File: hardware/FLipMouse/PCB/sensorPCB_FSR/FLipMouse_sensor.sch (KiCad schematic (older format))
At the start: 9 parts, among them J1 Conn_02x05_Odd_Even, J2 FSR1, J3 FSR1, J4 FSR2, J5 FSR2, J6 FSR3, J7 FSR3, J8 FSR4, J9 FSR4

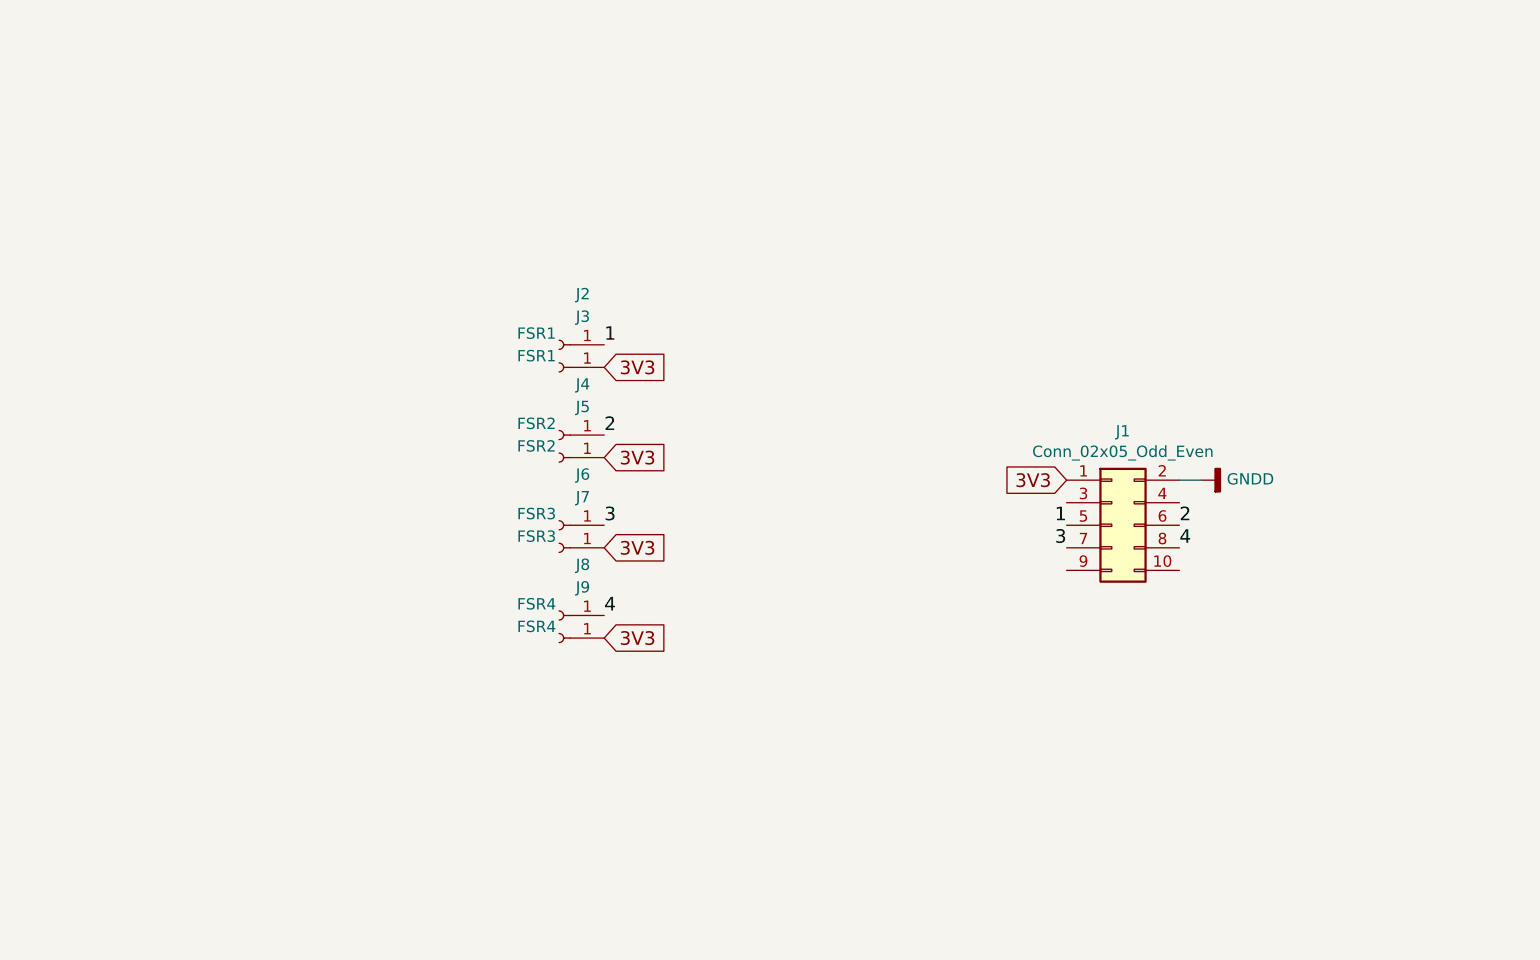
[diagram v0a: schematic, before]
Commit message: Added MEMS microphone to sensor PCB for voice recognition. Added production information
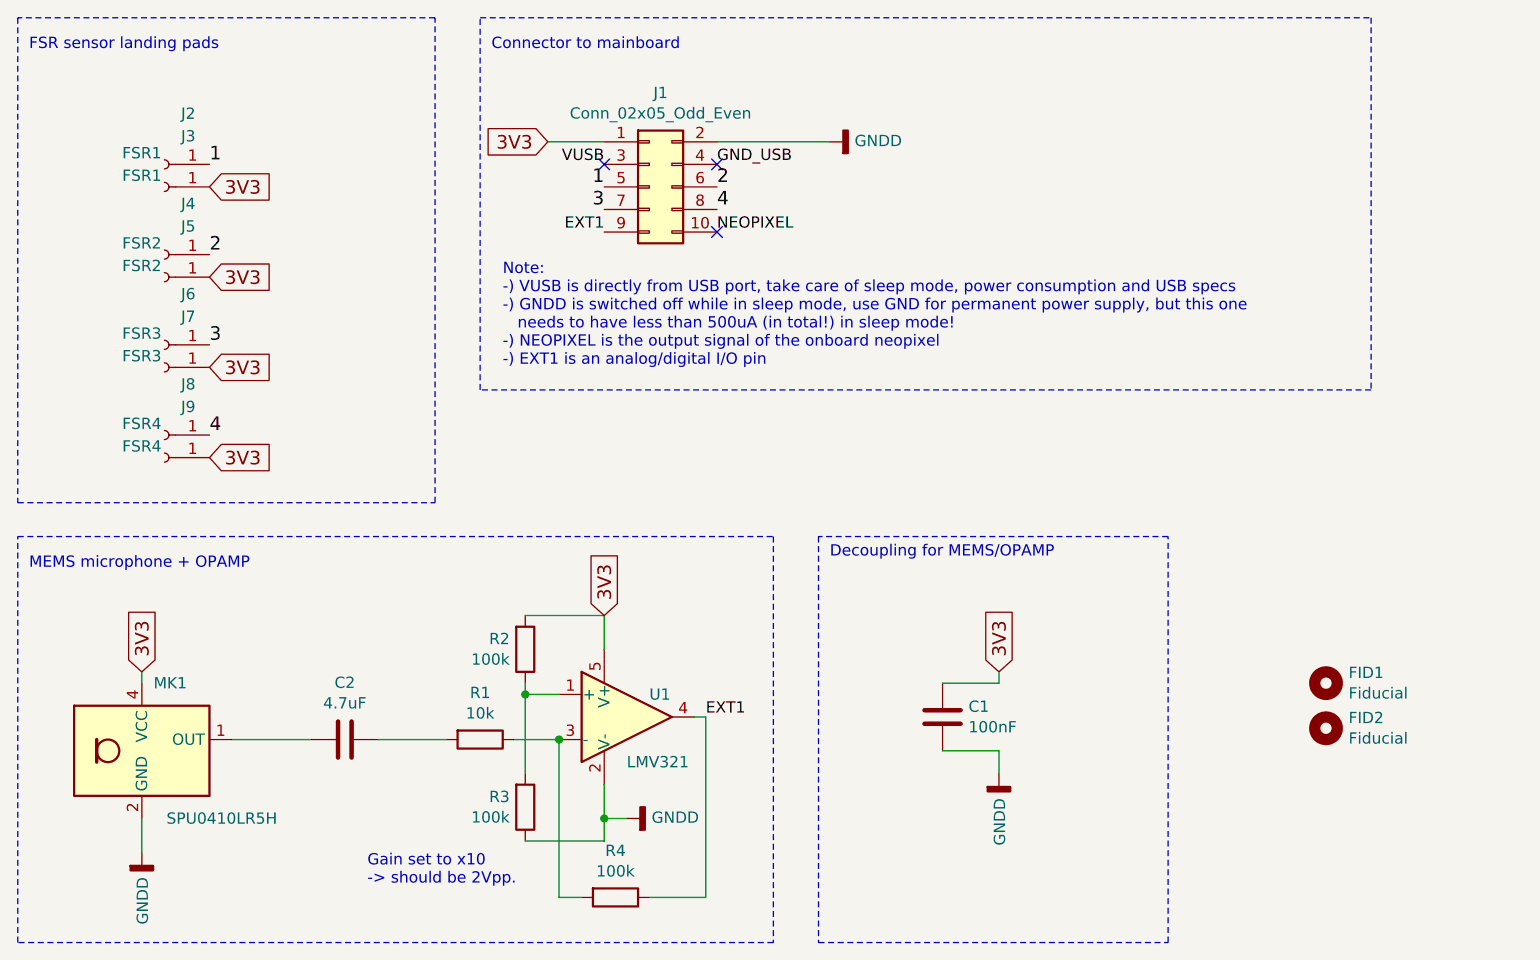
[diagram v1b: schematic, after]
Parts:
- added C1: 100nF, Capacitor_SMD:C_0603_1608Metric, symbol Device:C
- added C2: 4.7uF, Capacitor_SMD:C_0603_1608Metric, symbol Device:C
- added FID1, FID2: Fiducial, Fiducial:Fiducial_0.5mm_Dia_1mm_Outer, symbol Mechanical:MountingHole
- added MK1: SPU0410LR5H, SPU0410:SPU0410LR5H_6_3.76x3mm, symbol SPU0410:SPU0410LR5H
- added R1: 10k, Resistor_SMD:R_0603_1608Metric, symbol Device:R
- added R2, R3, R4: 100k, Resistor_SMD:R_0603_1608Metric, symbol Device:R
- added U1: LMV321, Package_TO_SOT_SMD:SOT-23-5, symbol Amplifier_Operational:LMV321
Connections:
- net 3V3: now also C1.1, MK1.4 (VCC), R2.2, U1.5 (V+)
- net GNDD: now also C1.2, MK1.2 (GND), MK1.3 (GND), MK1.5 (GND), MK1.6 (GND), R3.1, U1.2 (V-)
- net NEOPIXEL: now reaches J1.10 (Pin_10)
- net VUSB: now reaches J1.3 (Pin_3)
- net GND_USB: now reaches J1.4 (Pin_4)
- net EXT1: now reaches J1.9 (Pin_9)
- net EXT1: now also R4.1, U1.4
- new net: C2.2, MK1.1 (OUT)
- new net: R1.1, R4.2, U1.3 (-)
- new net: R2.1, R3.2, U1.1 (+)
- new net: C2.1, R1.2
- no-connect marks 0 -> 3
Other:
- note added: "Connector to mainboard"
- note added: "Decoupling for MEMS/OPAMP"
- note added: "FSR sensor landing pads"
- note added: "Gain set to x10\n-> should be 2Vpp."
- note added: "MEMS microphone + OPAMP"
- note added: "Note:\n-) VUSB is directly from USB port, take care of sleep mode, power consumption and USB specs\n-) GNDD is switched off while in sleep mode, use GND for permanent power supply, but this one \n needs to have less than 500uA (in total!) in sleep mode!\n-) NEOPIXEL is the output signal of the onboard neopixel\n-) EXT1 is an analog/digital I/O pin"
- moved on the sheet: J1, J2, J3, J4, J5, J6, J7, J8, J9
